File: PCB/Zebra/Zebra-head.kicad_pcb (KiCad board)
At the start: 2 copper layers, 38.1 x 43.2 mm, 4 parts, among them J1 Conn_01x11, J2 Conn_01x11, U1 ProMicro, U2 ssd1306

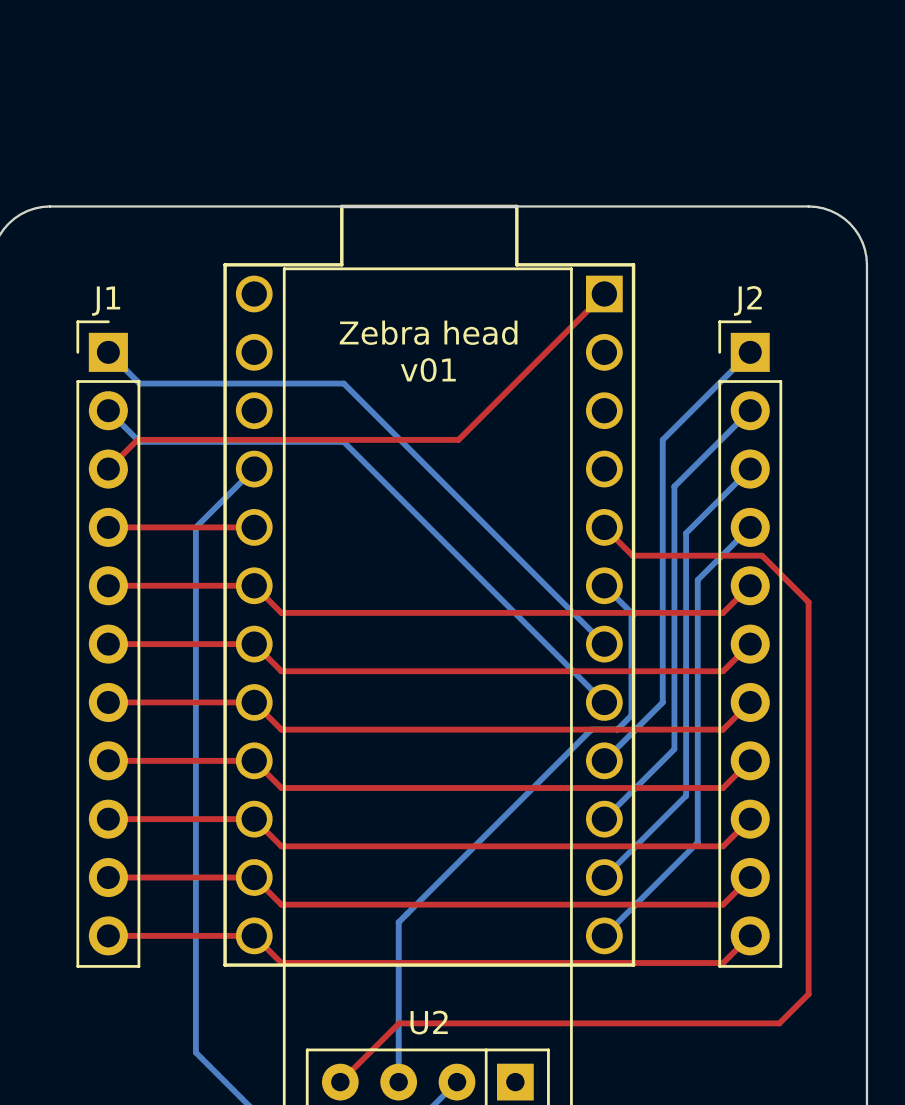
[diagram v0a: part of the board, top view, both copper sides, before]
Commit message: Switch to foostan's footprint library, MIT license
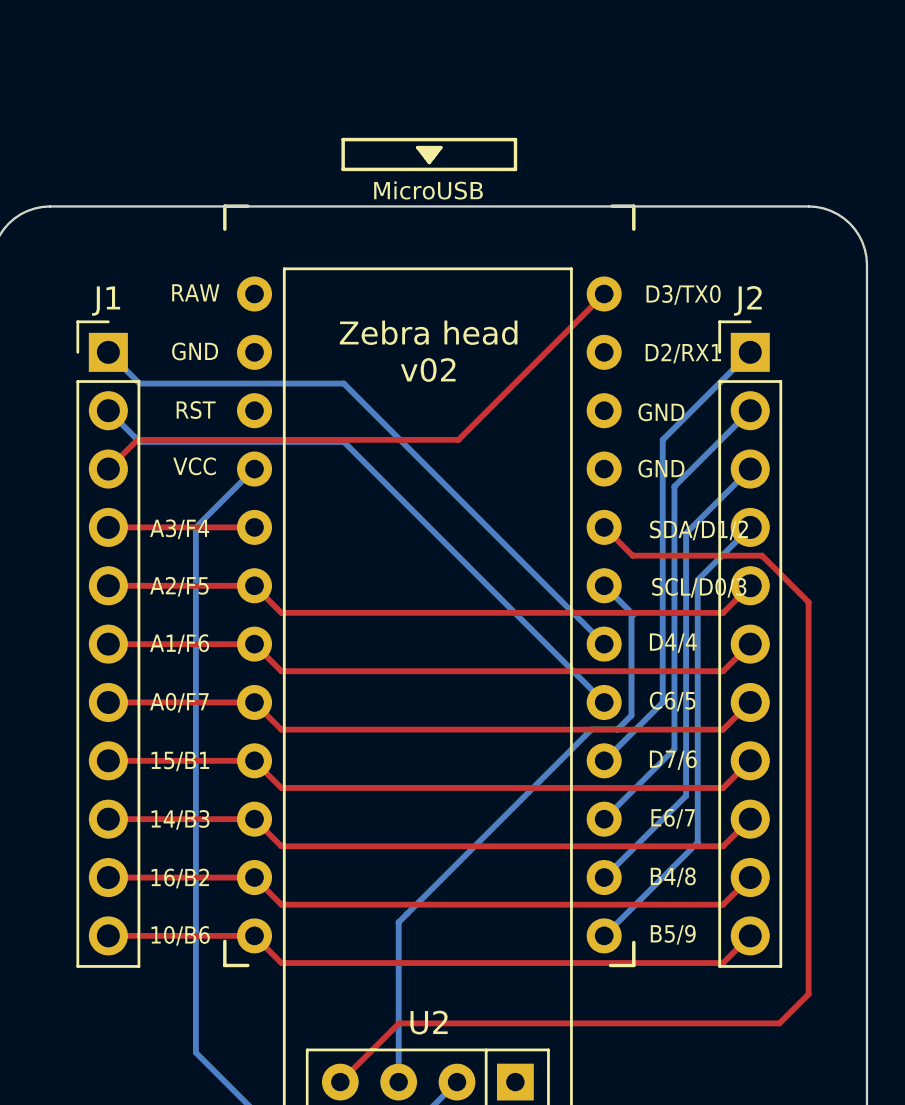
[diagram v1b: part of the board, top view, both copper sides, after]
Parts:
- U1: footprint promicro:ProMicro-DualFootprint -> kbd:ProMicro_v3.5; moved to F.Cu
- moved U1 0.51 mm to (94.0, 107.2), turned to 0 degrees
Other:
- board text added: "Zebra head v02"
- board text removed: "Zebra head v01"

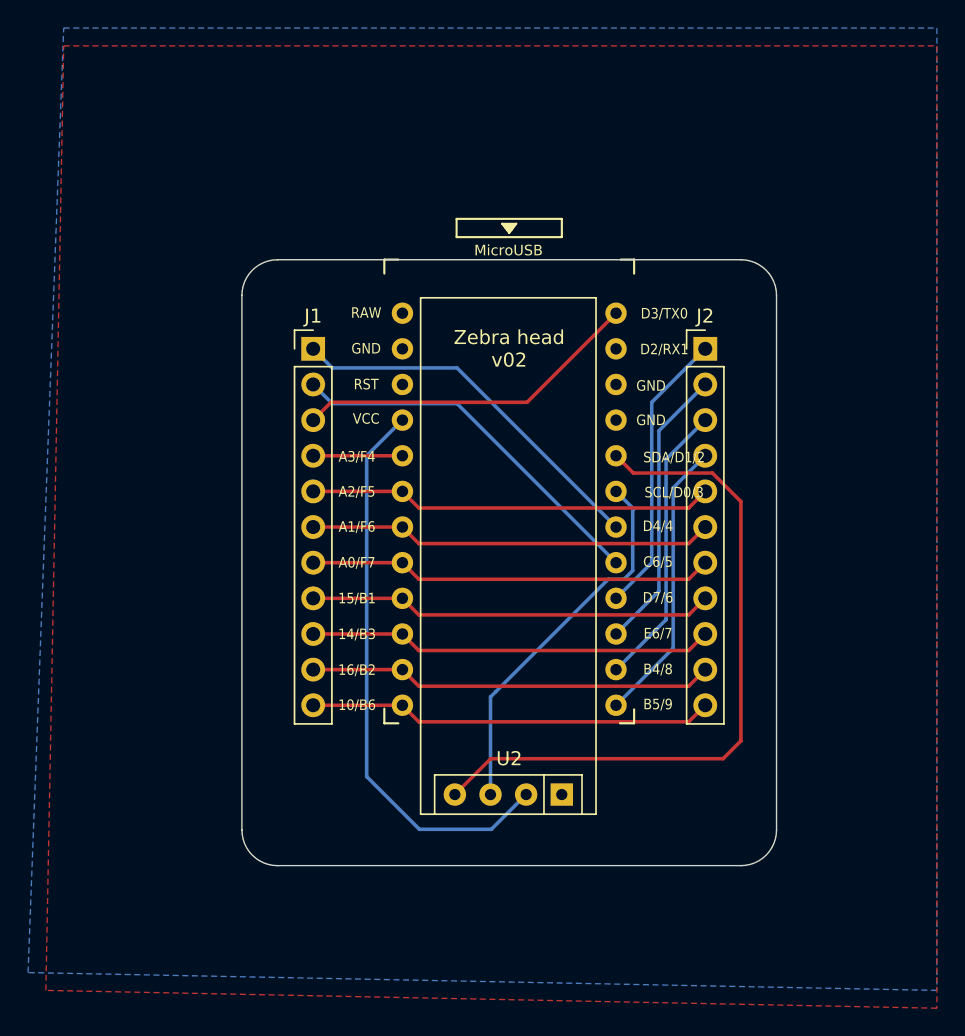
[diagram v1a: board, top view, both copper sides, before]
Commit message: Add TRRS jack
With serial and optional I2C
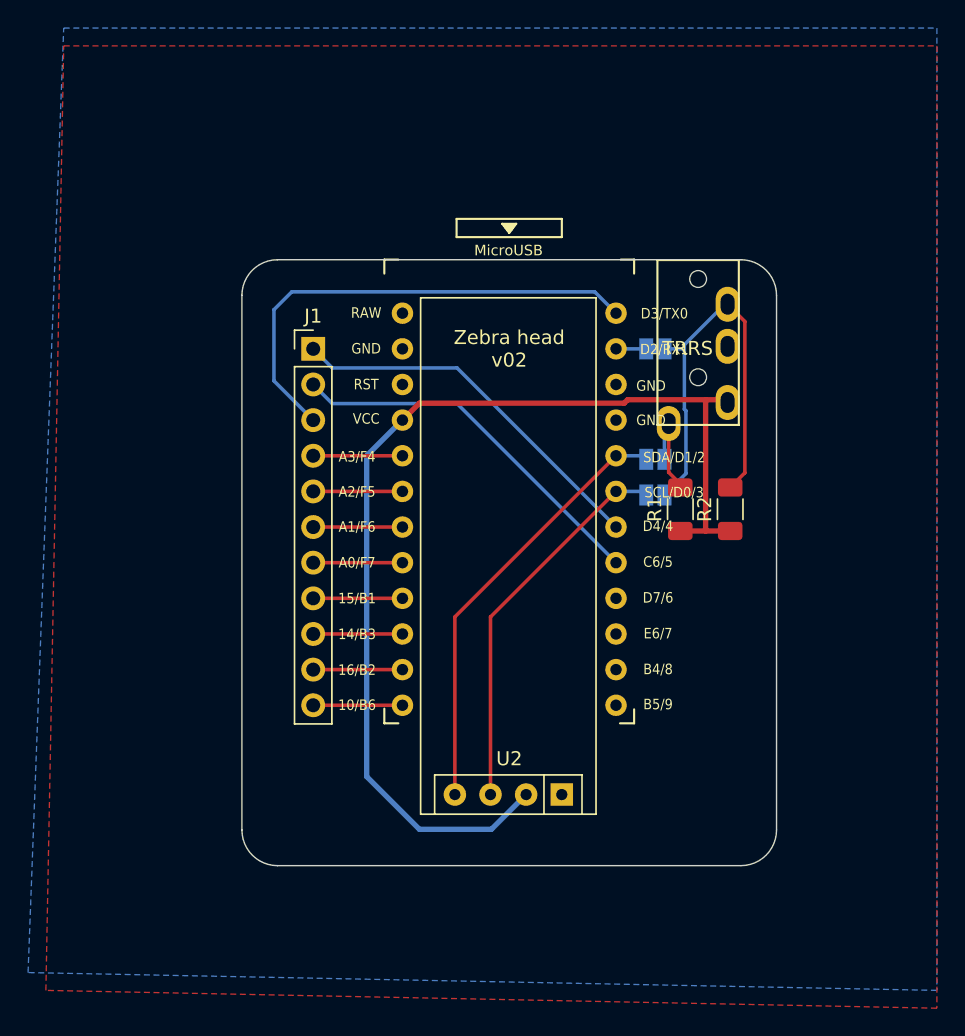
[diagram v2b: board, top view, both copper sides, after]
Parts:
- added JP1: Jumper_NO_Small, Jumper:SolderJumper-2_P1.3mm_Open_Pad1.0x1.5mm, B.Cu at (104.4, 103.1)
- added JP2: Jumper_NO_Small, Jumper:SolderJumper-2_P1.3mm_Open_Pad1.0x1.5mm, B.Cu at (104.4, 105.7)
- added JP3: Jumper_NC_Small, Jumper:SolderJumper-2_P1.3mm_Bridged_Pad1.0x1.5mm, B.Cu at (104.4, 95.2)
- added R1: 6k, Resistor_SMD:R_1206_3216Metric_Pad1.30x1.75mm_HandSolder, F.Cu at (106.2, 106.7)
- added R2: 6k, Resistor_SMD:R_1206_3216Metric_Pad1.30x1.75mm_HandSolder, F.Cu at (109.7, 106.7)
- J2: value Conn_01x11 -> MJ-4PP-9; footprint Connector_PinHeader_2.54mm:PinHeader_1x11_P2.54mm_Vertical -> kbd:MJ-4PP-9_1side
- moved J2 6.50 mm to (107.4, 88.8)
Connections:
- net Net-(U1-Pad5) renamed SDA
- net Net-(U1-Pad6) renamed SCL
- U1 pad 10: Net-(J2-Pad2) -> Net-(U1-Pad10)
- U1 pad 11: Net-(J2-Pad3) -> Net-(U1-Pad11)
- U1 pad 12: Net-(J2-Pad4) -> Net-(U1-Pad12)
- U1 pad 2: Net-(U1-Pad2) -> Serial
- U1 pad 9: Net-(J2-Pad1) -> Net-(U1-Pad9)
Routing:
- net VCC: track 40.4 -> 76.9 mm
- net Net-(J2-PadB): track 0.00 -> 31.0 mm
- net Net-(J1-Pad9): track 28.9 -> 6.35 mm
- net Net-(J1-Pad7): track 28.9 -> 6.35 mm
- net Net-(J1-Pad5): track 28.9 -> 6.35 mm
- net Net-(J1-Pad8): track 28.9 -> 6.35 mm
- net Net-(J1-Pad6): track 28.9 -> 6.35 mm
- net Net-(J1-Pad11): track 28.9 -> 6.35 mm
- net Net-(J1-Pad10): track 28.9 -> 6.35 mm
- net Net-(J2-Pad4): track 20.4 -> 0.00 mm
- net Net-(J2-Pad3): track 20.4 -> 0.00 mm
- net Net-(J2-Pad1): track 20.4 -> 0.00 mm
- net Net-(J2-Pad2): track 20.4 -> 0.00 mm
- net SDA: track 49.3 -> 31.5 mm
- net Net-(J1-Pad3): track 24.7 -> 34.6 mm
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
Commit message: Revert "Add TRRS jack"
This reverts commit 0ecc4aa986bd018de9fb38d5a9cbe8efcda9557b.
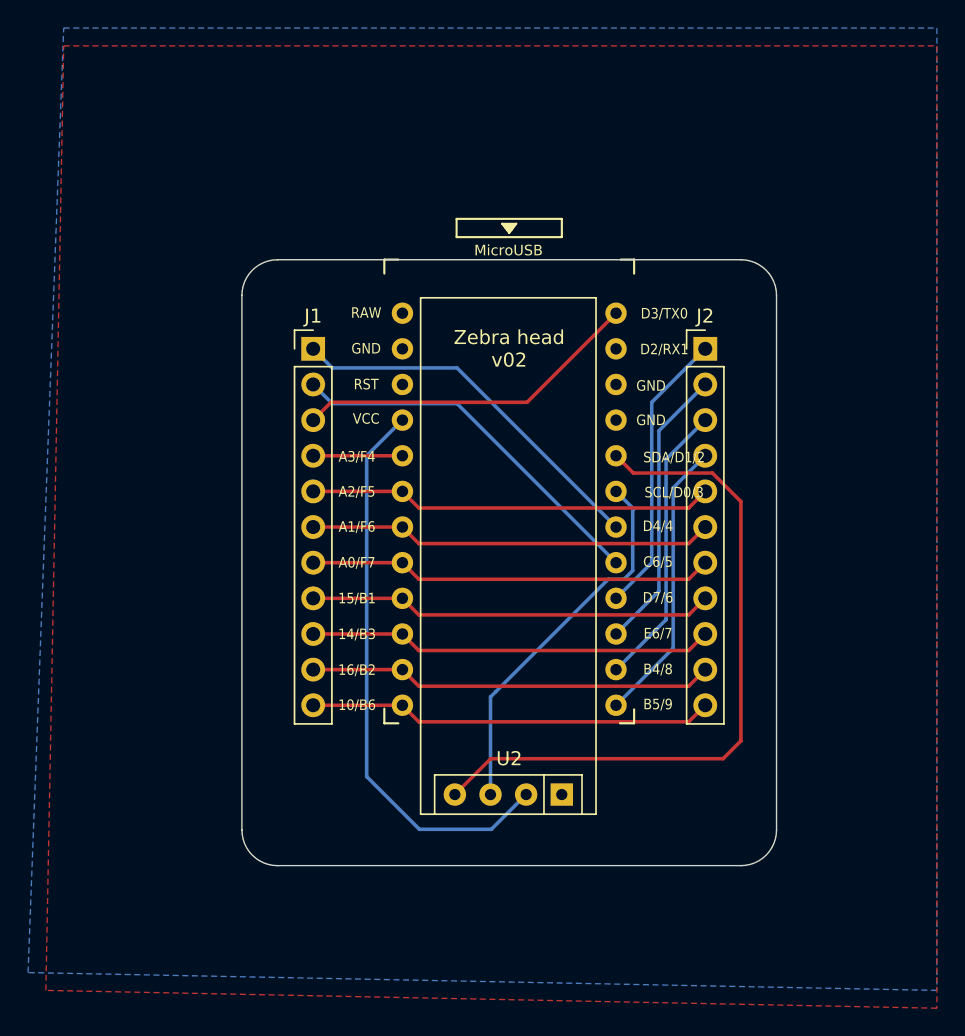
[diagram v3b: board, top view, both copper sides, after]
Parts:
- removed JP1, JP2: Jumper_NO_Small, Jumper:SolderJumper-2_P1.3mm_Open_Pad1.0x1.5mm
- removed JP3: Jumper_NC_Small, Jumper:SolderJumper-2_P1.3mm_Bridged_Pad1.0x1.5mm
- removed R1, R2: 6k, Resistor_SMD:R_1206_3216Metric_Pad1.30x1.75mm_HandSolder
- J2: value MJ-4PP-9 -> Conn_01x11; footprint kbd:MJ-4PP-9_1side -> Connector_PinHeader_2.54mm:PinHeader_1x11_P2.54mm_Vertical
- moved J2 6.50 mm to (108.0, 95.2)
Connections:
- net SCL renamed Net-(U1-Pad6)
- net SDA renamed Net-(U1-Pad5)
- U1 pad 10: Net-(U1-Pad10) -> Net-(J2-Pad2)
- U1 pad 11: Net-(U1-Pad11) -> Net-(J2-Pad3)
- U1 pad 12: Net-(U1-Pad12) -> Net-(J2-Pad4)
- U1 pad 2: Serial -> Net-(U1-Pad2)
- U1 pad 9: Net-(U1-Pad9) -> Net-(J2-Pad1)
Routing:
- net VCC: track 76.9 -> 40.4 mm
- net Net-(J2-PadB): track 31.0 -> 0.00 mm
- net Net-(J1-Pad9): track 6.35 -> 28.9 mm
- net Net-(J1-Pad7): track 6.35 -> 28.9 mm
- net Net-(J1-Pad5): track 6.35 -> 28.9 mm
- net Net-(J1-Pad8): track 6.35 -> 28.9 mm
- net Net-(J1-Pad6): track 6.35 -> 28.9 mm
- net Net-(J1-Pad11): track 6.35 -> 28.9 mm
- net Net-(J1-Pad10): track 6.35 -> 28.9 mm
- net Net-(J2-Pad4): track 0.00 -> 20.4 mm
- net Net-(J2-Pad3): track 0.00 -> 20.4 mm
- net Net-(J2-Pad1): track 0.00 -> 20.4 mm
- net Net-(J2-Pad2): track 0.00 -> 20.4 mm
- net Net-(U1-Pad5): track 31.5 -> 49.3 mm
- net Net-(J1-Pad3): track 34.6 -> 24.7 mm
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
